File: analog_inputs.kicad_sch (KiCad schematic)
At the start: 60 parts, among them J10 1862424, J11 1862424, J4 1862424, J5 1862424, J6 1862424, J7 1862424, J8 1862424, J9 1862424, U3 ADS1256IDBT, U4 REF5050IDGK, Y1 Crystal

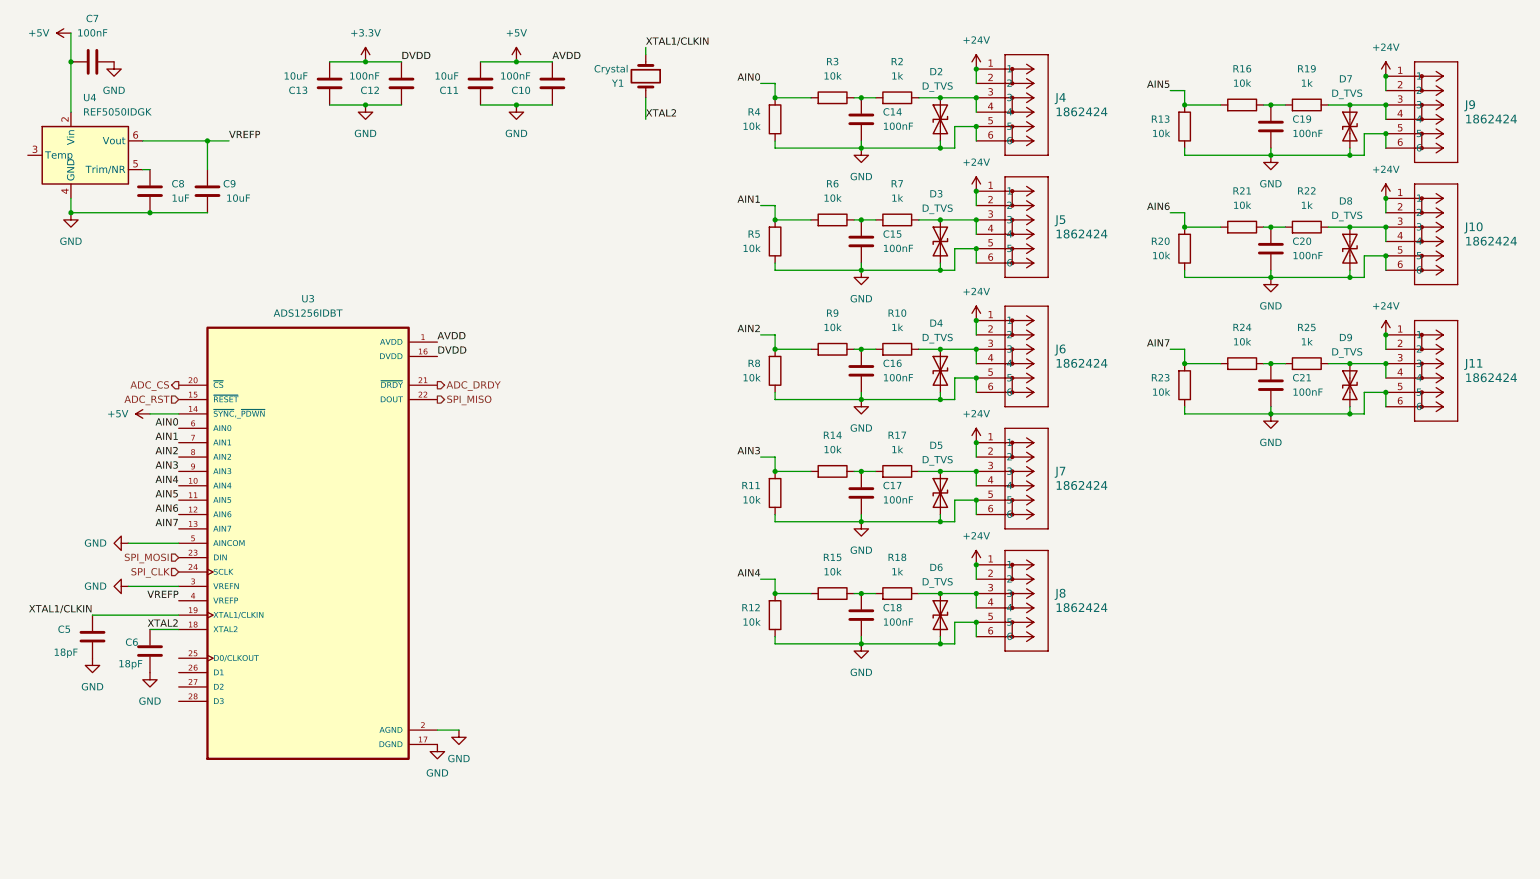
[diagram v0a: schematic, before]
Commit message: Updated schematic and PCB
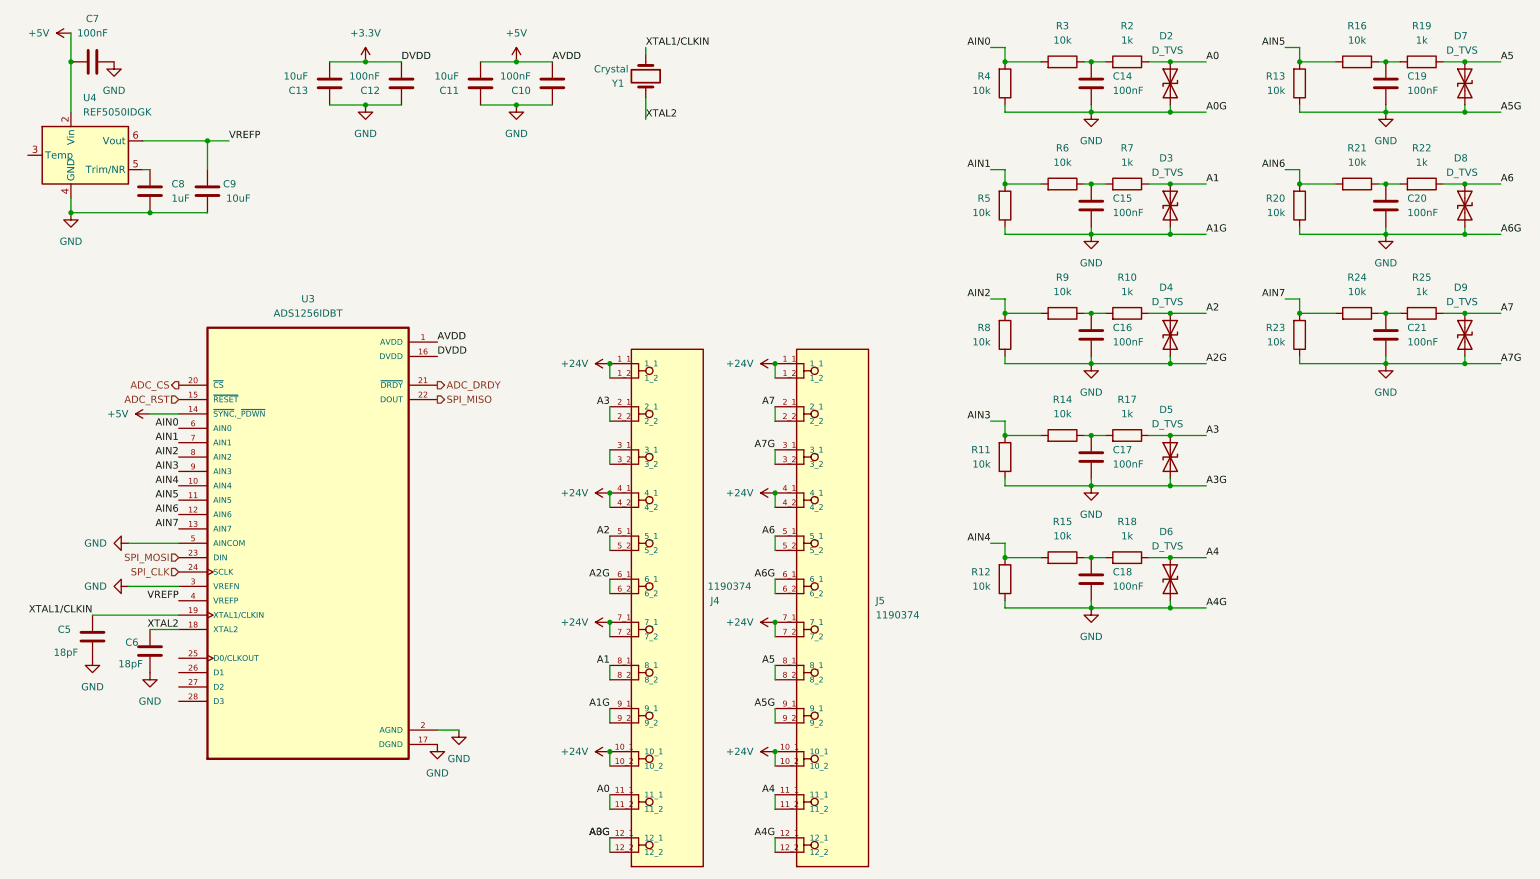
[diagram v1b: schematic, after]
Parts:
- removed J10, J11, J4, J5, J6, J7, J8, J9: 1862424, CONN_1862424, symbol 2026-03-28_19-29-49:1862424
- added J4, J5: 1190374, LPTA 2,512-5,0 - PCB terminal block1:PHOENIX_1190374, symbol 1190374:1190374
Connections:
- net +24V: now also J4.10_1, J4.10_2, J4.1_1, J4.1_2, J4.4_1, J4.4_2, J4.7_1, J4.7_2, J5.10_1, J5.10_2, J5.1_1, J5.1_2, J5.4_1, J5.4_2, J5.7_1, J5.7_2
- net GND: now also J4.12_1, J4.12_2, J4.6_1, J4.6_2, J4.9_1, J4.9_2, J5.12_1, J5.12_2, J5.3_1, J5.3_2, J5.6_1, J5.6_2, J5.9_1, J5.9_2
- net A4: now reaches D6.1 (A1), R18.1
- net A4: now also J5.11_1, J5.11_2
- net A7: now reaches D9.1 (A1), R25.1
- net A7: now also J5.2_1, J5.2_2
- net A6: now reaches D8.1 (A1), R22.1
- net A6: now also J5.5_1, J5.5_2
- net A2: now reaches D4.1 (A1), R10.1
- net A2: now also J4.5_1, J4.5_2
- net A1: now reaches D3.1 (A1), R7.1
- net A1: now also J4.8_1, J4.8_2
- net A0: now reaches D2.1 (A1), R2.1
- net A0: now also J4.11_1, J4.11_2
- net A5: now reaches D7.1 (A1), R19.1
- net A5: now also J5.8_1, J5.8_2
- net A3: now reaches D5.1 (A1), R17.1
- net A3: now also J4.2_1, J4.2_2
- new net: J4.3_1, J4.3_2
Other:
- moved on the sheet: C14, C15, C16, C17, C18, C19, C20, C21, D2, D3, D4, D5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
